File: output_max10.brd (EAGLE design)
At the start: 73.9 x 54.2 mm, 58 parts, among them IC4 IS61WV1288EEBLL-10HLI, IC5 10M04EQFP144

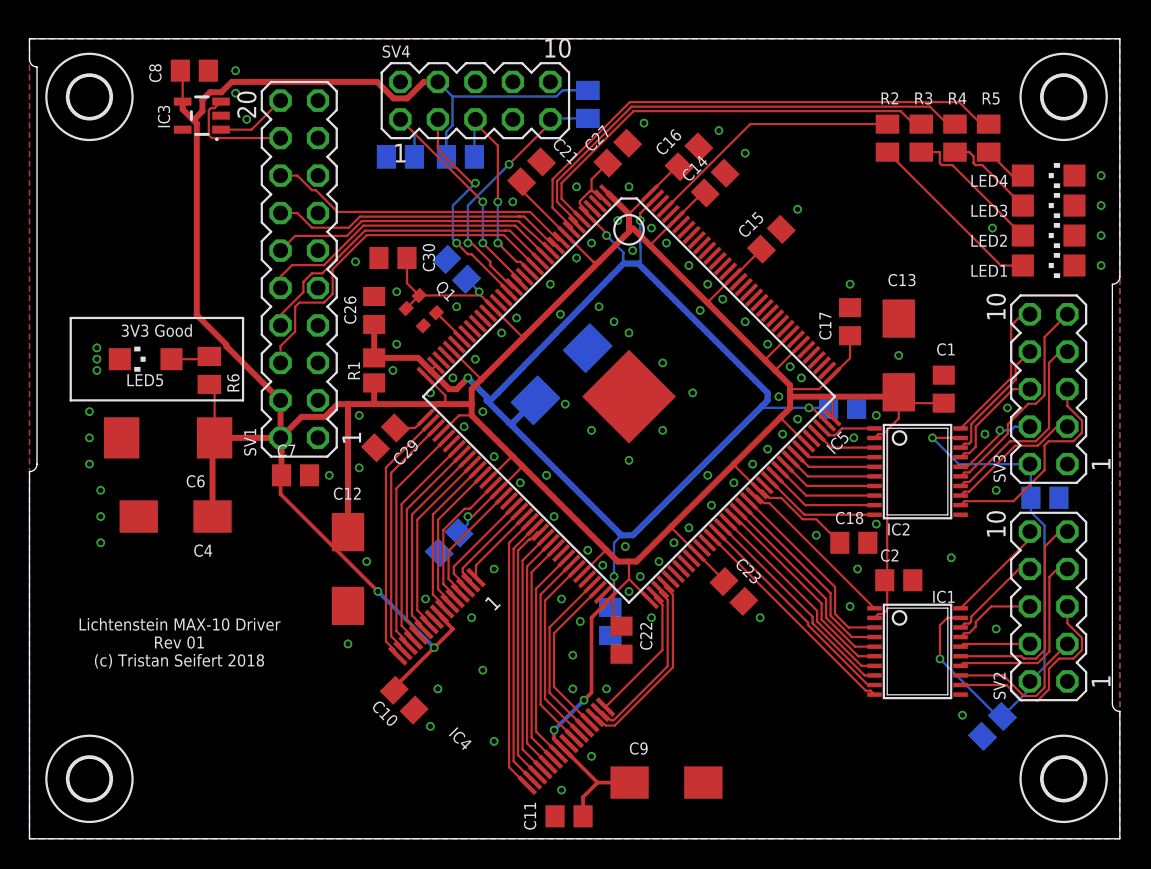
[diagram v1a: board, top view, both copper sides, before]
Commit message: Fixed some more footprints on MAX10 driver
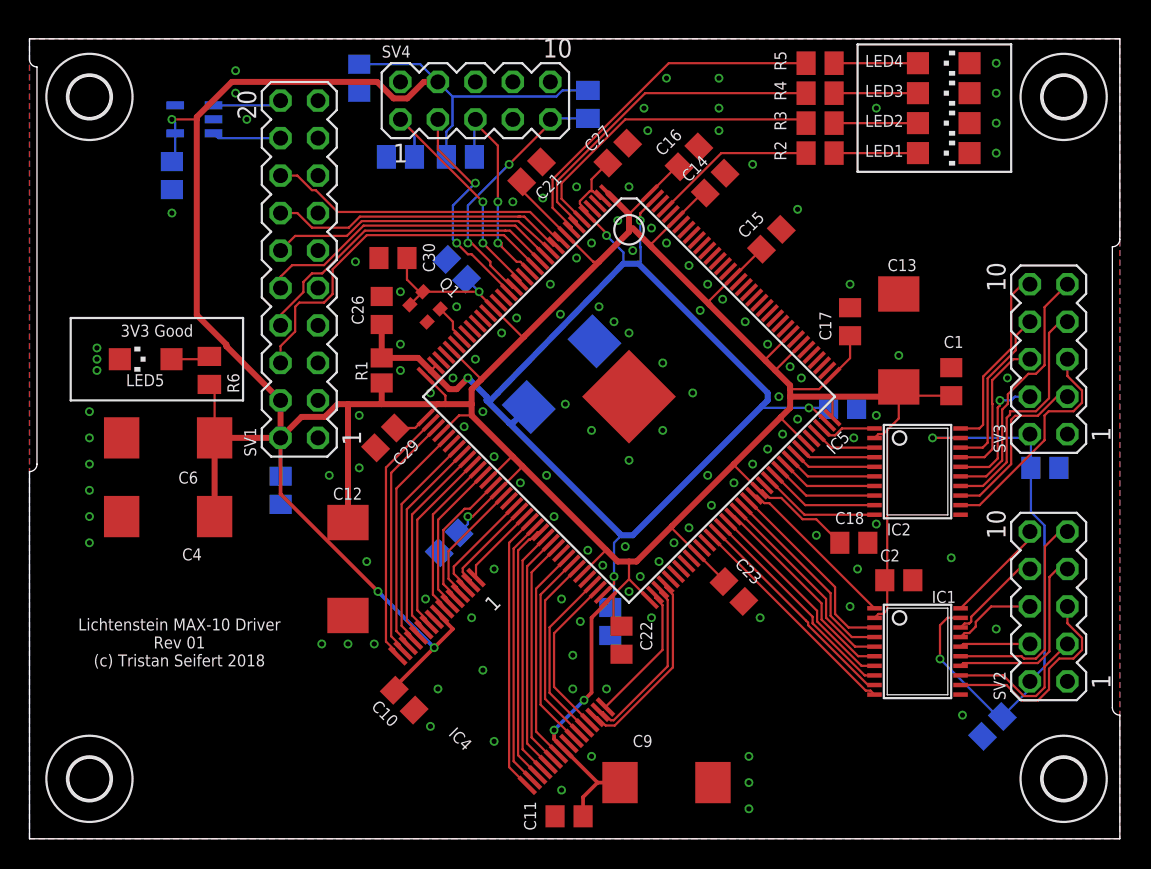
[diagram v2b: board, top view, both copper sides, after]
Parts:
- added C31: 100nF, rcl:C0805
- C12, C13, C25, C4, C9: value 47µF -> 100µF; device rcl:CT6032 -> rcl:SMC_D
- Q1: value (none) -> 25MHz
- moved R5 12.5 mm to (53.6, 52.6), turned to 0 degrees
- moved LED2 10.4 mm to (62.0, 48.5)
- moved LED4 10.4 mm to (62.0, 52.6)
- moved LED1 10.4 mm to (62.0, 46.5)
- moved LED3 10.4 mm to (62.0, 50.5)
- moved R4 9.64 mm to (53.6, 50.5), turned to 0 degrees
- moved C8 7.27 mm to (9.65, 45.0), flipped to the bottom, turned to 90 degrees
- moved R3 6.93 mm to (53.6, 48.5), turned to 0 degrees
- moved R2 4.68 mm to (53.6, 46.5), turned to 0 degrees
- moved C3 2.03 mm to (68.8, 25.1)
- moved SV3 2.03 mm to (69.1, 32.5)
- moved C7 1.44 mm to (17.0, 23.6), flipped to the bottom, turned to 270 degrees
- moved C13 1.02 mm to (58.9, 33.8)
- moved C1 0.72 mm to (62.5, 31.0)
- moved IC3 0.57 mm to (11.2, 48.8), flipped to the bottom, turned to 270 degrees
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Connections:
- net +3V3: now also C31.2
- net GND: now also C31.1
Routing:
- net STATUS3: track 36.3 -> 24.4 mm
- net STATUS2: track 33.1 -> 22.8 mm
- net +3V3: track 338.2 -> 346.7 mm, vias 6 -> 7
- net STATUS1: track 29.8 -> 21.5 mm
- net N$13: track 12.4 -> 5.68 mm
- net STATUS0: track 17.4 -> 11.1 mm
- net N$14: track 9.65 -> 5.68 mm
- net OUTPUT11: track 6.03 -> 9.53 mm
- net I2C_SDA: track 7.71 -> 4.67 mm
- net OUTPUT12: track 14.5 -> 17.3 mm
- net OUTPUT10: track 7.41 -> 10.2 mm
- net OUTPUT8: track 9.99 -> 12.8 mm
- net OUTPUT13: track 13.6 -> 16.3 mm
- net OUTPUT9: track 8.64 -> 11.4 mm
- net N$2: track 2.97 -> 5.68 mm
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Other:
- outline, holes or cut-outs redrawn

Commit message: clean up board some more; change eeprom to SOIC
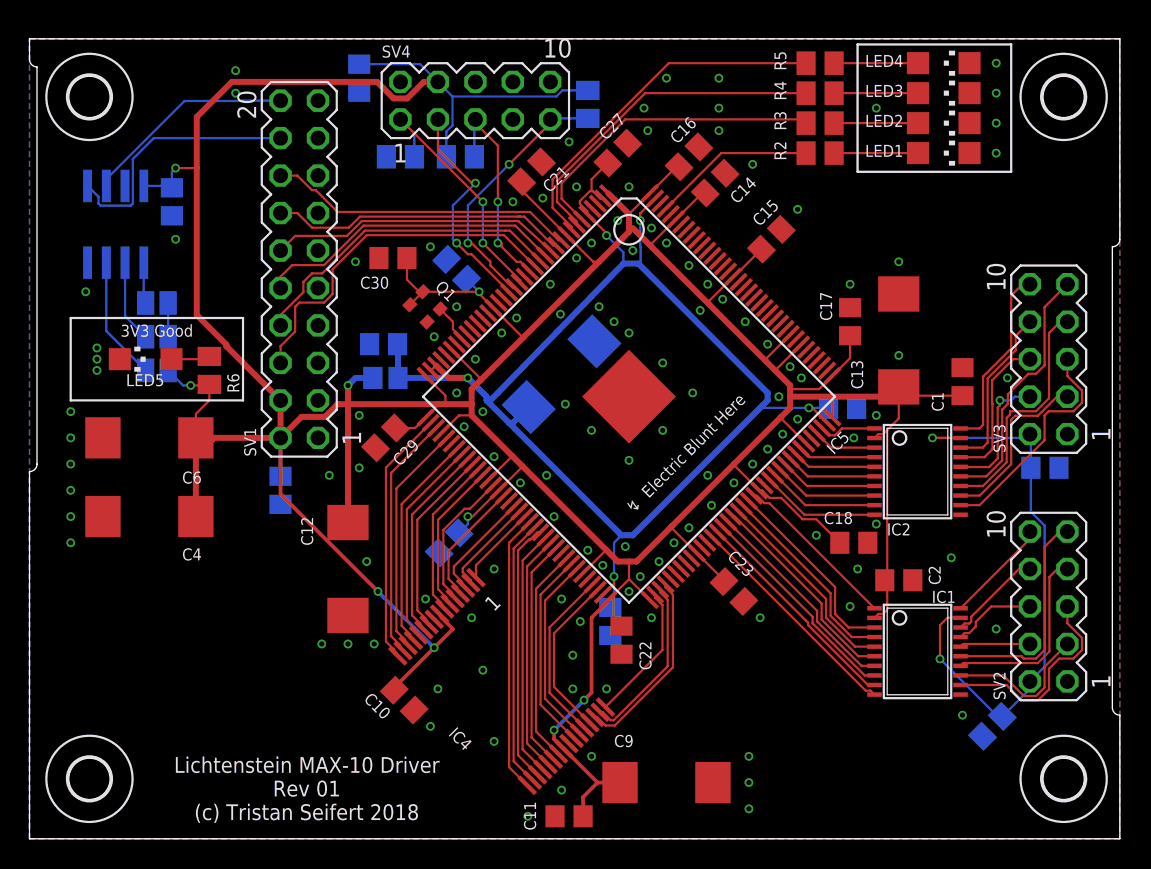
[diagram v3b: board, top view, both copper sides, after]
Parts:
- added SJ1, SJ2, SJ3: (no value), jumper:SJ
- IC3: device lichtenstein_onion:SOT23-5 -> lichtenstein_onion:SOIC8
- moved IC3 8.89 mm to (5.84, 41.7), turned to 0 degrees
- moved C26 2.29 mm to (24.0, 33.5), flipped to the bottom, turned to 0 degrees
- moved C8 1.78 mm to (9.65, 43.2)
- moved C4 1.27 mm to (8.13, 21.8)
- moved C6 1.27 mm to (8.13, 27.2)
- moved C1 0.76 mm to (63.2, 31.0)
- moved R1 0.57 mm to (24.1, 31.2), flipped to the bottom, turned to 180 degrees
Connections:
- new net N$5: IC3.3, SJ1.2
- new net N$6: IC3.2, SJ2.2
- new net N$7: IC3.1, SJ3.2
- net +3V3: now also IC3.8, SJ1.1, SJ2.1, SJ3.1; no longer IC3.4
- net GND: now also IC3.4; no longer IC3.2
- net I2C_SCL: now also IC3.6; no longer IC3.1
- net I2C_SDA: now also IC3.5; no longer IC3.3
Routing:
- net +3V3: track 346.7 -> 359.7 mm, vias 7 -> 9
- net I2C_SDA: track 4.67 -> 17.6 mm
- net I2C_SCL: track 4.67 -> 14.5 mm
- net N$5: track 0.00 -> 8.41 mm
- net N$6: track 0.00 -> 5.60 mm
- net N$7: track 0.00 -> 2.79 mm
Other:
- board text added: "↯ Electric Blunt Here"

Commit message: Fixed bulk capacitor footprints; made +V for output channels independent on output board
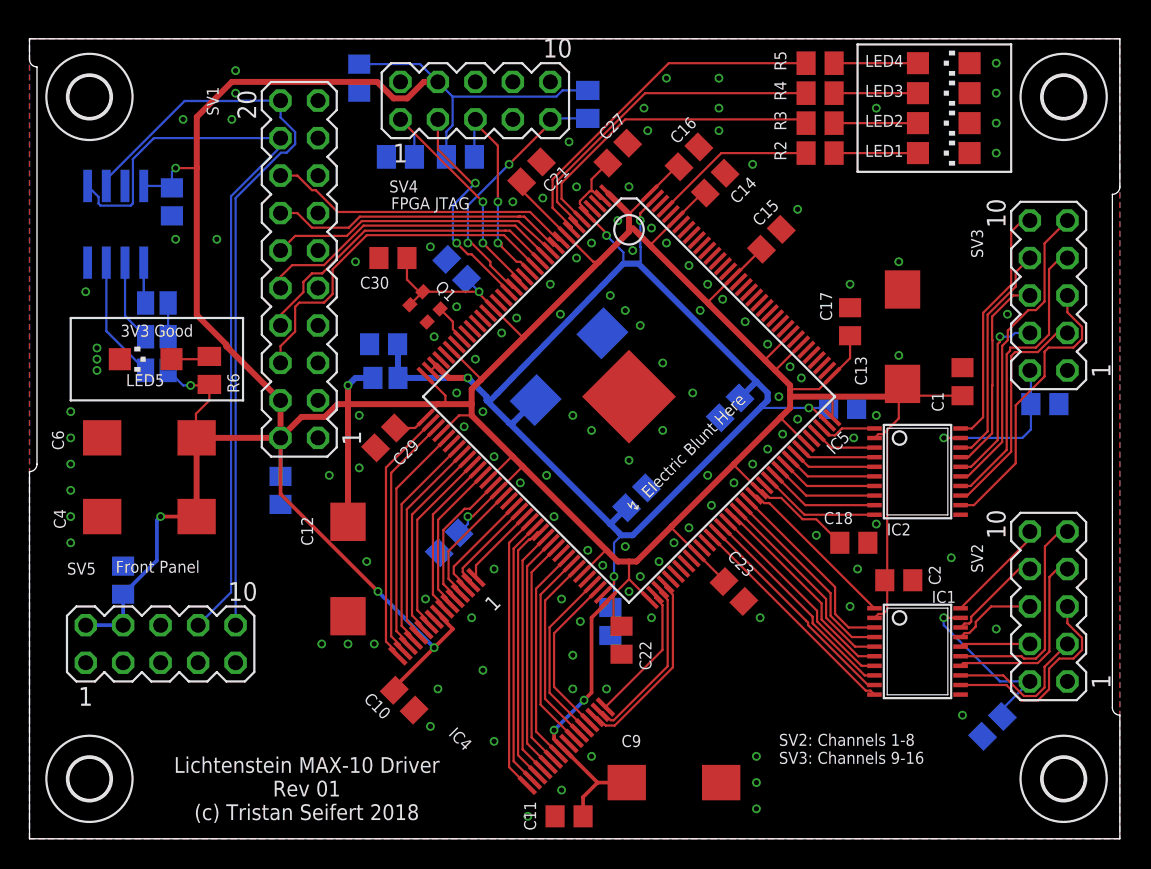
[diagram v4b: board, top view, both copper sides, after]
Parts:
- added C32, C33, C34: 100nF, rcl:C0805
- added SV5: (no value), con-lstb:MA05-2
- C12, C13, C25, C4, C9: value 100µF -> 47µF; device rcl:SMC_D -> rcl:CT7343
- C6: device rcl:SMC_D -> rcl:CT7343
- moved C3 4.32 mm to (68.8, 29.5)
- moved SV3 4.32 mm to (69.1, 36.8)
- moved C25 0.72 mm to (36.6, 32.0)
- moved C9 0.51 mm to (43.7, 3.81)
- moved C13 0.36 mm to (59.2, 34.0)
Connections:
- removed net V+: C3.1, C5.1, IC1.19, IC2.19, SV2.2, SV3.2
- new net V+0: C5.1, IC1.19, SV2.2
- new net V+1: C3.1, IC2.19, SV3.2
- net +3V3: now also C33.1, SV5.2, SV5.4
- net GND: now also C32.2, C33.2, C34.2, SV5.1, SV5.3
- net I2C_SCL: now also SV5.10
- net I2C_SDA: now also SV5.8
- net VCCA: now also C32.1, C34.1
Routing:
- net V+: track 39.2 -> 0.00 mm, vias 2 -> 0
- net I2C_SCL: track 14.5 -> 52.3 mm
- net I2C_SDA: track 17.6 -> 52.9 mm
- net +3V3: track 359.7 -> 374.0 mm, vias 9 -> 10
- net V+0: track 0.00 -> 12.2 mm, vias 0 -> 1
- net V+1: track 0.00 -> 11.3 mm, vias 0 -> 1
- net OUTPUT15: track 15.5 -> 19.5 mm
- net OUTPUT8: track 12.8 -> 16.8 mm
- net OUTPUT9: track 11.4 -> 15.2 mm
- net OUTPUT13: track 16.3 -> 20.2 mm
- net OUTPUT14: track 11.8 -> 15.6 mm
- net VCCA: track 95.4 -> 99.2 mm
- net OUTPUT10: track 10.2 -> 13.9 mm
- net OUTPUT11: track 9.53 -> 13.1 mm
- net OUTPUT12: track 17.3 -> 20.9 mm
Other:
- outline, holes or cut-outs redrawn
- board text added: "FPGA JTAG"
- board text added: "Front Panel"
- board text added: "SV2: Channels 1-8 SV3: Channels 9-16"

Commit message: Cleaned up output board; added pull-ups to inputs on Lichtenstein board; moved some decoupling caps on FPGA output board
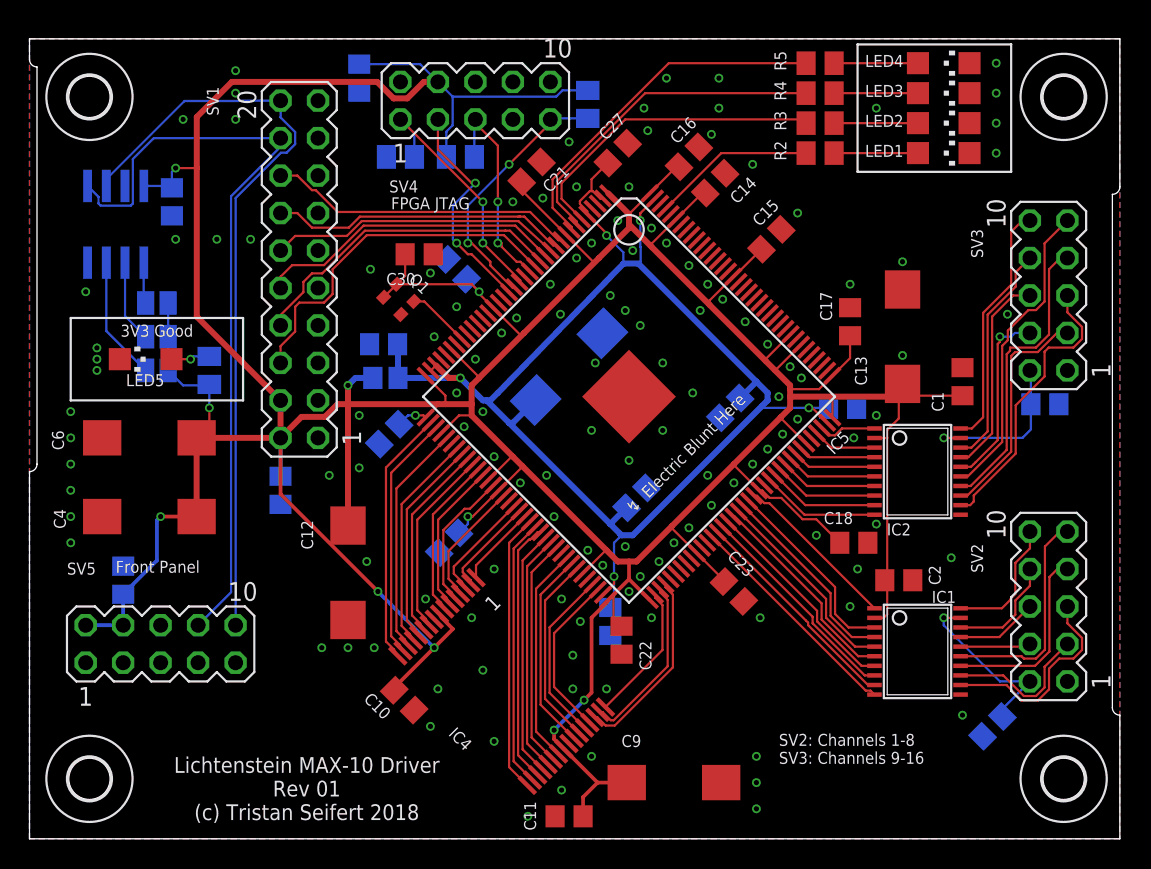
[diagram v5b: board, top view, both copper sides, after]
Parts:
- moved Q1 1.85 mm to (24.9, 37.6)
- moved C30 1.80 mm to (26.4, 39.6), turned to 0 degrees
- moved C29 0.36 mm to (24.4, 27.4), flipped to the bottom, turned to 315 degrees
- moved C12 0.25 mm to (21.6, 18.0)
- flipped R6 to the bottom
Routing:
- net CLKIN_24: track 2.67 -> 4.39 mm
- net OUTPUT0: track 7.15 -> 8.79 mm
- net OUTPUT1: track 6.53 -> 7.58 mm
- net +3V3: track 374.0 -> 375.0 mm, vias 10 -> 11
- net VCCA: track 99.2 -> 98.6 mm
- net N$3: track 2.70 -> 2.65 mm, vias 0 -> 1

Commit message: Added some required reisstors to FPGA outputboard
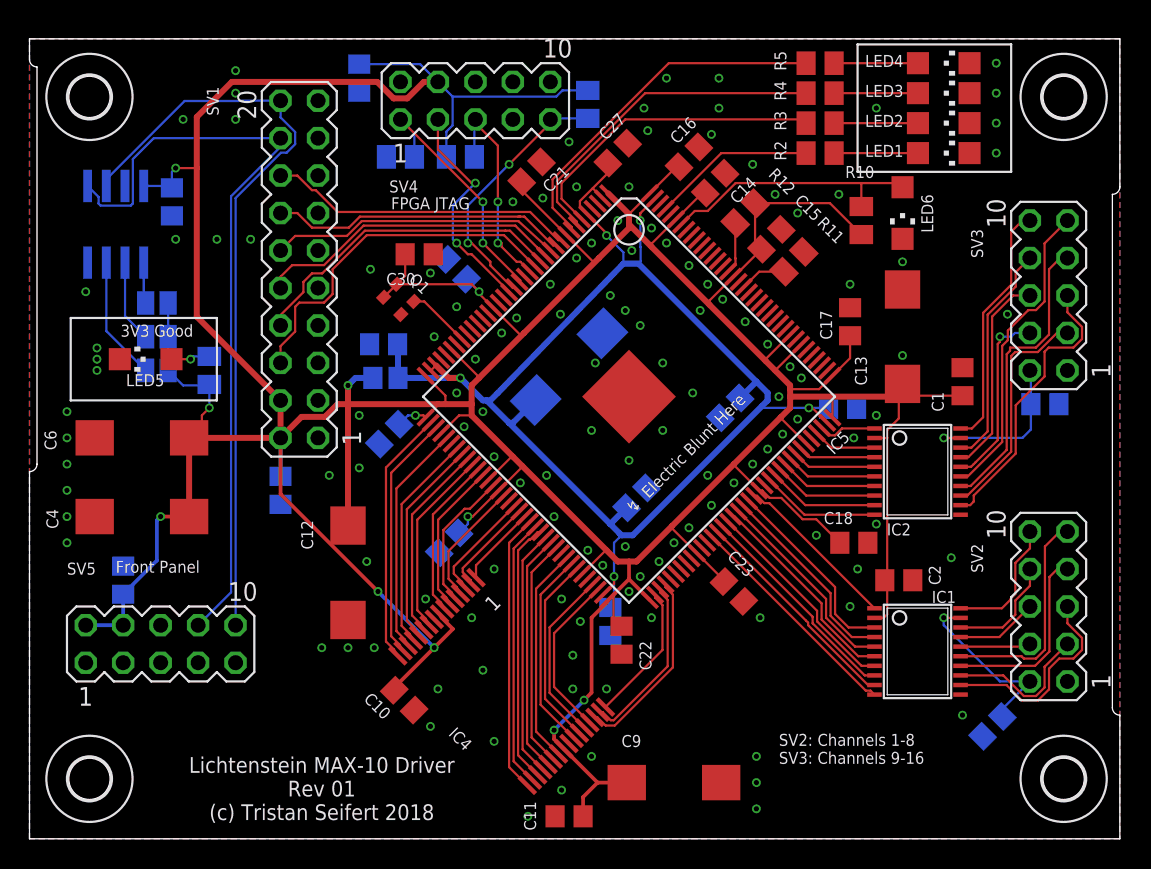
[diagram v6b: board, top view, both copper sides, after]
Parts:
- added LED6: (no value), led:CHIPLED_1206
- added R10: 10k/680R??, rcl:M0805
- added R11, R12: 10k, rcl:M0805
- moved C4 0.51 mm to (7.62, 21.8)
- moved C6 0.51 mm to (7.62, 27.2)
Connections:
- new net !CONFIG: IC5.129, R12.2
- new net !DEV_CLR: IC5.121
- new net !STATUS: IC5.136
- new net CONFIG_SEL: IC5.126, R11.2
- new net CONF_DONE: IC5.138, LED6.A, R10.2
- new net CRC_ERROR: IC5.134
- new net DEV_OE: IC5.122
- net +3V3: now also R10.1, R12.1
- net GND: now also IC5.26, IC5.27, IC5.28, IC5.32, IC5.33, LED6.C, R11.1
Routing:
- net CONF_DONE: track 0.00 -> 18.0 mm
- net +3V3: track 375.0 -> 385.5 mm
- net !CONFIG: track 0.00 -> 3.50 mm
- net CONFIG_SEL: track 0.00 -> 3.16 mm

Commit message: rev 01 of fpga output board
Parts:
- moved C9 2.03 mm to (45.7, 3.81)
- moved C17 1.78 mm to (55.6, 36.8)
- moved C23 1.27 mm to (48.8, 16.0)
- moved C22 0.51 mm to (40.1, 13.0)
- moved C14 0.36 mm to (46.7, 44.7)
- moved C15 0.36 mm to (50.5, 40.9)
- moved C16 0.36 mm to (45.0, 46.5)
- moved R11 0.36 mm to (52.1, 39.4)
- moved R12 0.36 mm to (48.8, 42.7)
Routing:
- net +3V3: track 385.5 -> 392.6 mm
- net SRAM_A16: track 9.41 -> 12.0 mm
- net SRAM_A15: track 11.7 -> 13.3 mm
- net SRAM_A14: track 13.0 -> 14.5 mm
